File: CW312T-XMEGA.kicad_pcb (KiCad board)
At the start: 2 copper layers, 58.7 x 53.7 mm, 7 parts, among them P1 PCIEx4 EDGE CONNECTOR, U1 ATXMEGA128D4-AU

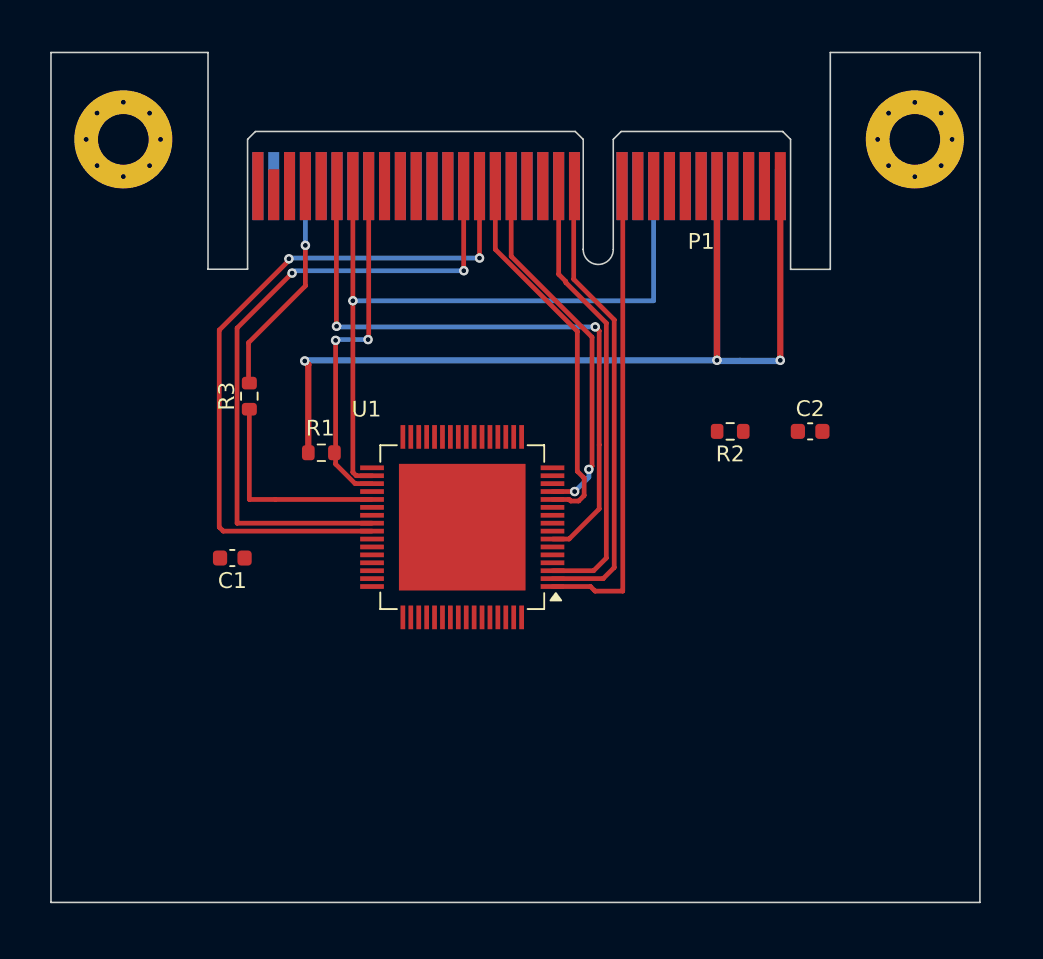
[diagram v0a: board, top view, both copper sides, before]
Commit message: Draft of CW312T-XMEGA target - ready for review
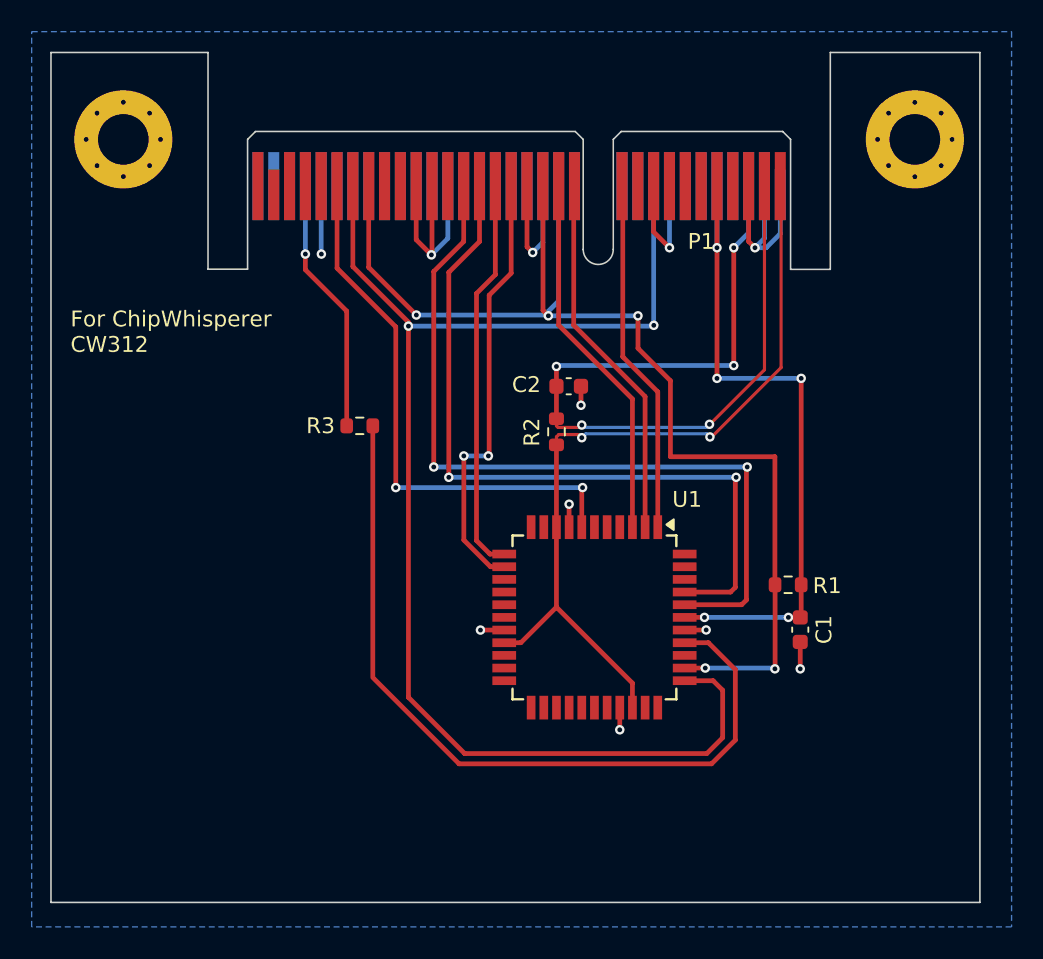
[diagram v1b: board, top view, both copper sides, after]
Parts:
- added PCB1: CE, Silkscrren_Symbols:CE-Logo_8.5x6mm_SilkScreen, F.Cu at (138.6, 107.3)
- added PCB2: Pb_Free, Silkscrren_Symbols:Pb_Free_8.0x8.0mm_SilkScreen, F.Cu at (127.6, 107.5)
- added PCB3: WEEE, Silkscrren_Symbols:WEEE-Logo_5.6x8mm_SilkScreen, F.Cu at (146.4, 107.2)
- U1: footprint Package_QFP:TQFP-64-1EP_10x10mm_P0.5mm_EP8x8mm -> Package_QFP:TQFP-44_10x10mm_P0.8mm
- moved C1 36.2 mm to (170.4, 95.9), turned to 90 degrees
- moved R1 30.6 mm to (169.7, 93.1), turned to 0 degrees
- moved C2 15.5 mm to (155.8, 80.5)
- moved R2 11.0 mm to (155.1, 83.4), turned to -90 degrees
- moved U1 10.1 mm to (157.4, 95.2), turned to -90 degrees
- moved R3 7.22 mm to (142.6, 83.0), turned to 180 degrees
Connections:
- net /PDIC renamed /HDR5/RST
- P1 pad B1: VCC -> VCC CLEAN
- R2 pad 2: VCC -> VCC CLEAN
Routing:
- net GND: track 0.00 -> 56.4 mm, vias 0 -> 11
- net /HDR5/RST: track 22.4 -> 75.8 mm, vias 2 -> 5
- net Net-(P1-FILT_LP): track 0.00 -> 53.2 mm, vias 0 -> 5
- net VCC CLEAN: track 0.00 -> 51.1 mm, vias 0 -> 2
- net /PDID: track 45.6 -> 85.5 mm, vias 1 -> 2
- net /CLK: track 13.5 -> 50.0 mm
- net VCC: track 69.0 -> 44.2 mm, vias 3 -> 5
- net /GPIO4: track 42.0 -> 50.8 mm
- net /LED1: track 30.1 -> 22.5 mm
- net /CLKOUT: track 41.1 -> 34.9 mm
- net /LED2: track 29.3 -> 23.4 mm
- net /LED3: track 28.5 -> 23.5 mm
- net /GPIO1: track 23.3 -> 27.8 mm
- net /GPIO3: track 45.1 -> 47.6 mm
- net Net-(P1-CLKIN): track 14.0 -> 16.4 mm
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- added copper zone on B.Cu, net GND
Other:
- board text added: "For ChipWhisperer CW312"
- board text added: "NewAE Technology Inc. NAE-CW312T-XMEGA RoHS / PB-Free"

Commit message: added production files
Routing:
- net GND: track 56.4 -> 52.1 mm, vias 11 -> 10
- net /PDID: vias 2 -> 1
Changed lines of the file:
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@@
 			(outputformat 1)
 			(mirror no)
-			(drillshape 1)
+			(drillshape 0)
 			(scaleselection 1)
 			(outputdirectory "")
@@
 		(tags "resistor")
 		(property "Reference" "R1"
-			(at 2.465 0.06 360)
+			(at 2.465 0.06 0)
 			(layer "F.SilkS")
 			(effects
@@
 		)
 		(property "Value" "RES_10k_0603"
-			(at 0 1.43 360)
+			(at 0 1.43 0)
 			(layer "F.Fab")
 			(effects
@@
 		)
 		(fp_text user "${REFERENCE}"
-			(at 0 0 360)
+			(at 0 0 0)
 			(layer "F.Fab")
 			(effects
@@
 		(tags "capacitor")
 		(property "Reference" "C2"
-			(at -2.675 -0.1 360)
+			(at -2.675 -0.1 0)
 			(layer "F.SilkS")
 			(effects
@@
 		)
 		(property "Value" "CAP_100n_6.3V_0603"
-			(at 0 1.43 360)
+			(at 0 1.43 0)
 			(layer "F.Fab")
 			(effects
@@
 		)
 		(fp_text user "${REFERENCE}"
-			(at 0 0 360)
+			(at 0 0 0)
 			(layer "F.Fab")
 			(effects
@@
 		(tags "resistor")
 		(property "Reference" "R3"
-			(at 2.475 0 360)
+			(at 2.475 0 0)
 			(layer "F.SilkS")
 			(effects
@@
 		)
 		(property "Value" "RES_100R_0603"
-			(at 0 1.43 360)
+			(at 0 1.43 0)
 			(layer "F.Fab")
 			(effects
@@
 		)
 		(fp_text user "${REFERENCE}"
-			(at 0 0 360)
+			(at 0 0 0)
 			(layer "F.Fab")
 			(effects
@@
 	)
 	(via
-		(at 140.2 72.2)
-		(size 0.6)
-		(drill 0.3)
-		(layers "F.Cu" "B.Cu")
-		(net 2)
-	)
-	(via
 		(at 164.505731 95.942985)
 		(size 0.6)
@@
 	)
 	(segment
-		(start 140.19 72.19)
-		(end 140.19 67.905)
-		(width 0.3)
-		(layer "B.Cu")
-		(net 2)
-	)
-	(segment
-		(start 140.2 72.2)
-		(end 140.19 72.19)
-		(width 0.3)
-		(layer "B.Cu")
-		(net 2)
-	)
-	(segment
 		(start 154.19 71.46)
 		(end 154.19 67.905)
@@
 		(net 13)
 	)
-	(via
-		(at 161.2 76.7)
-		(size 0.6)
-		(drill 0.3)
-		(layers "F.Cu" "B.Cu")
-		(net 13)
-	)
 	(segment
 		(start 161.2 76.7)
@@
 		(polygon
 			(pts
-				(xy 121.9 58.15) (xy 183.8 58.15) (xy 183.8 114.7) (xy 183.8 114.7) (xy 121.9 114.7) (xy 121.9 114.7)
-				(xy 121.9 58.15)
+				(xy 121.9 58.15) (xy 183.8 58.15) (xy 183.8 114.7) (xy 121.9 114.7)
 			)
 		)

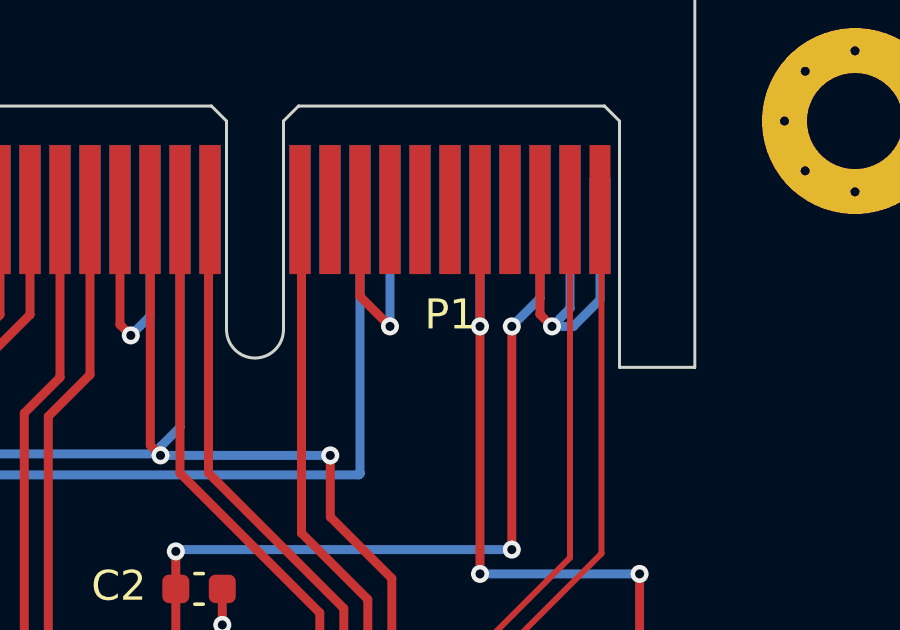
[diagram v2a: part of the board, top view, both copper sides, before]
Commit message: updated silkscreen and schematic
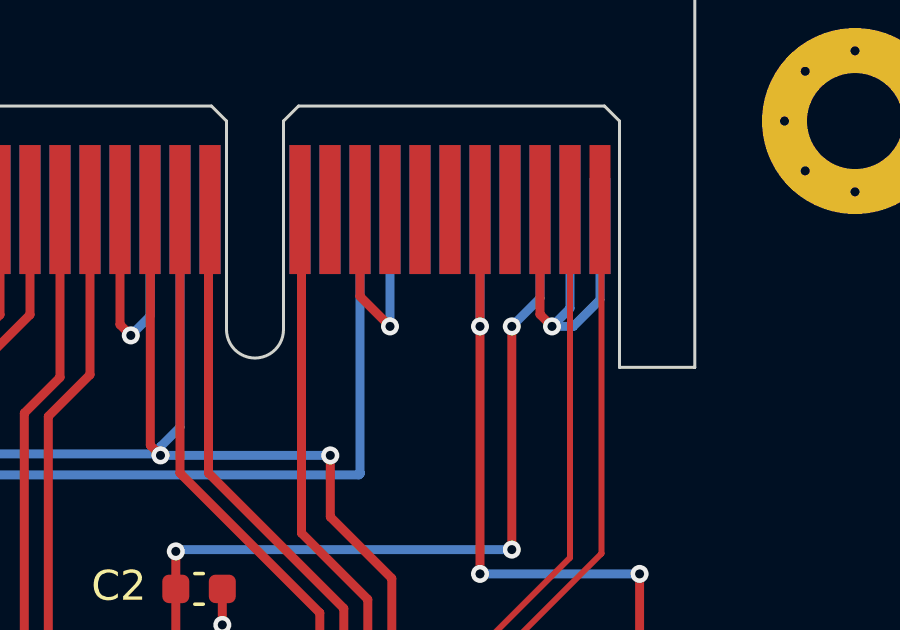
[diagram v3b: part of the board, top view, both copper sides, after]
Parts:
- added PCB4: WEEE SYMBOL, Silkscrren_Symbols:WEEE-Logo_5.6x8mm_SilkScreen, F.Cu at (127.1, 97.9)
- PCB1: value CE -> CE Symbol
- PCB2: value Pb_Free -> Pb_Free Symbol
- PCB3: value WEEE -> UKCA symbol; footprint Silkscrren_Symbols:WEEE-Logo_5.6x8mm_SilkScreen -> Silkscrren_Symbols:UKCA-Logo_8x8mm_SilkScreen
- moved PCB3 12.1 mm to (137.4, 99.1)
